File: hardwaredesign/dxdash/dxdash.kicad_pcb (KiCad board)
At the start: 2 copper layers, 133 parts, among them J1 Conn_01x08_Pin, J10 Screw_Terminal_01x04, J11 Screw_Terminal_01x04, J12 CAN, J16 uC_NRST, J17 3V3_uC, J18 SWO, J2 Conn_01x06_Pin, J3 Screw_Terminal_01x04, J4 DEBUG, J5 UART, J6 12V_in, J7 Screw_Terminal_01x04, J8 Power Low Side Outputs, J9 Screw_Terminal_01x04, Q1 NCV8402xST, Q2 NCV8402xST, Q3 NCV8402xST, Q4 BC556, Q6 BC546, Q7 BC556, Q8 BC546, SW1 SW_Push, SW2 SW_Push, SW3 SW_Push, SW4 SW_Push, SW5 SW_Push, U2 SN65HVD234, U3 STM32F103RETx, U4 TPS54302, U6 AMS1117-3.3, U7 74HCT04, Y2 8MHz

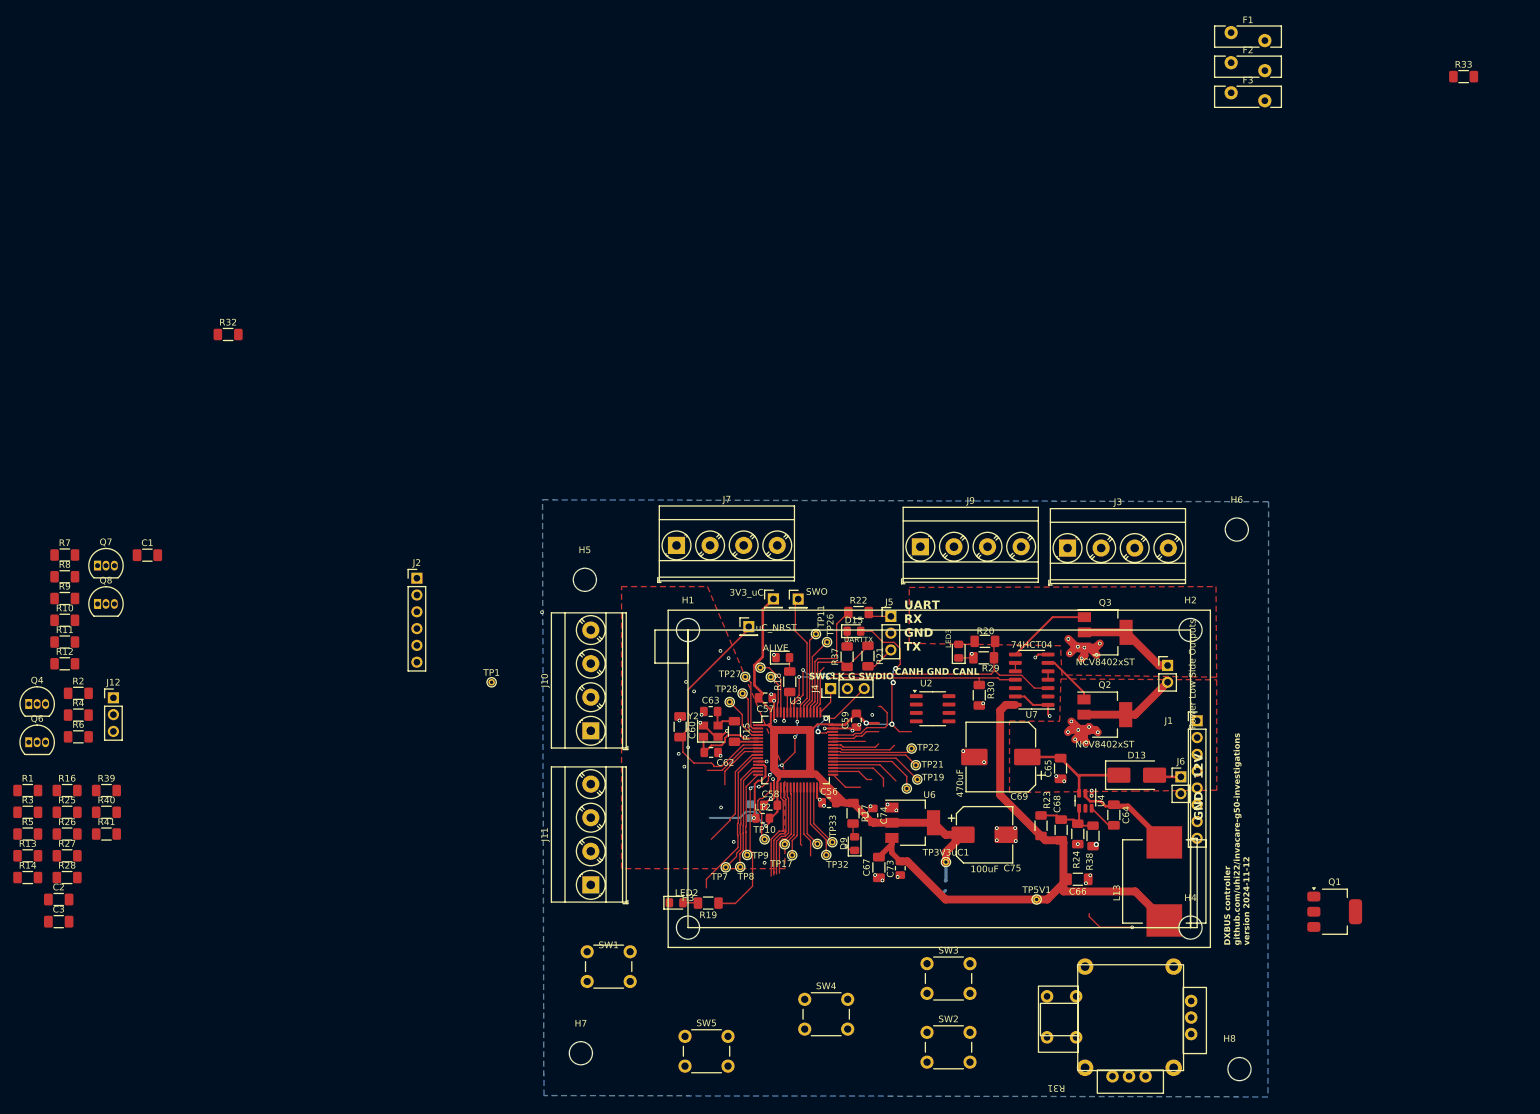
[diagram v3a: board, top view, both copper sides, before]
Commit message: added switch inputs. Layout preparation.
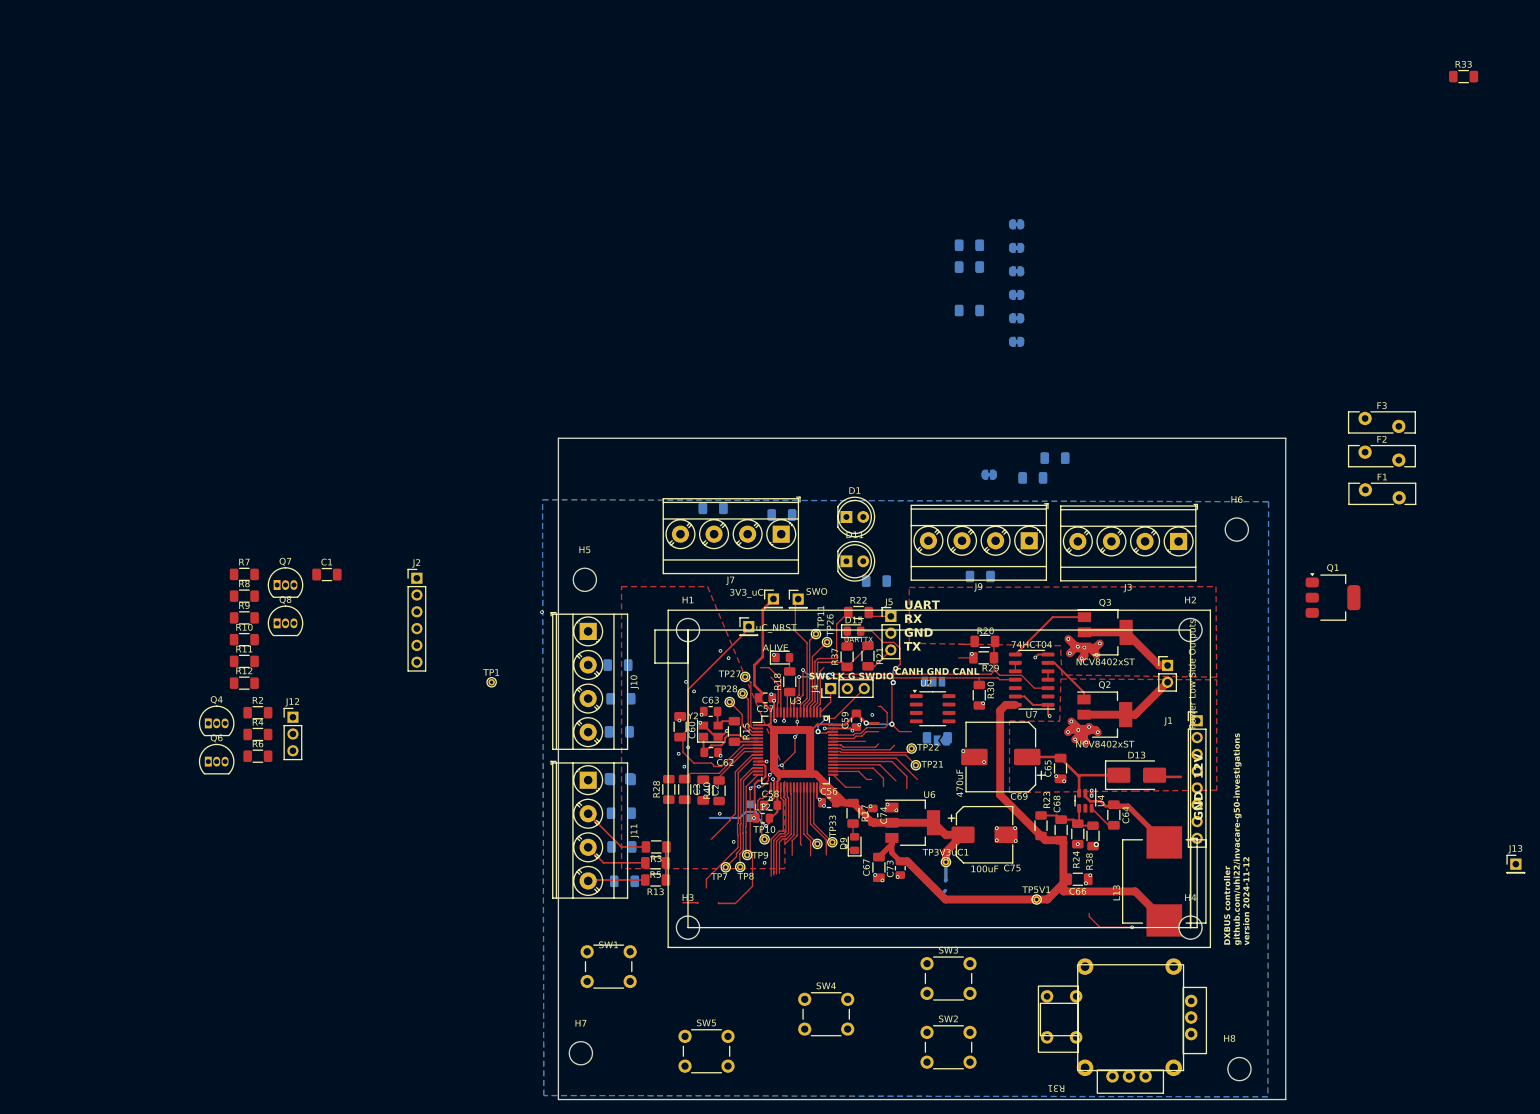
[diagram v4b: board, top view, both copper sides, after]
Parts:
- removed D12: LED3, LED_SMD:LED_0805_2012Metric_Pad1.15x1.40mm_HandSolder
- removed J6: 12V_in, Connector_PinHeader_2.54mm:PinHeader_1x02_P2.54mm_Vertical
- removed TP16, TP17, TP18, TP19, TP30, TP31, TP32: ~, TestPoint:TestPoint_THTPad_D1.0mm_Drill0.5mm
- added D1: LED2, LED_THT:LED_D5.0mm, F.Cu at (163.8, 71.7)
- added J13: Conn_01x01_Pin, Connector_PinHeader_2.54mm:PinHeader_1x01_P2.54mm_Vertical, F.Cu at (265.0, 124.2)
- added JP1: SolderJumper_2_Bridged, Jumper:SolderJumper-2_P1.3mm_Bridged_RoundedPad1.0x1.5mm, B.Cu at (189.5, 27.4)
- added JP2: SolderJumper_2_Bridged, Jumper:SolderJumper-2_P1.3mm_Bridged_RoundedPad1.0x1.5mm, B.Cu at (189.5, 31.0)
- added JP3: SolderJumper_2_Bridged, Jumper:SolderJumper-2_P1.3mm_Bridged_RoundedPad1.0x1.5mm, B.Cu at (189.5, 34.5)
- added JP4: SolderJumper_2_Open, Jumper:SolderJumper-2_P1.3mm_Open_TrianglePad1.0x1.5mm, B.Cu at (178.2, 105.5)
- added JP5: SolderJumper_3_Open, Jumper:SolderJumper-3_P1.3mm_Open_Pad1.0x1.5mm_NumberLabels, B.Cu at (176.9, 96.6)
- added JP6: SolderJumper_2_Bridged, Jumper:SolderJumper-2_P1.3mm_Bridged_RoundedPad1.0x1.5mm, B.Cu at (189.5, 38.1)
- added JP7: SolderJumper_2_Bridged, Jumper:SolderJumper-2_P1.3mm_Bridged_RoundedPad1.0x1.5mm, B.Cu at (189.5, 41.6)
- added JP8: SolderJumper_2_Bridged, Jumper:SolderJumper-2_P1.3mm_Bridged_RoundedPad1.0x1.5mm, B.Cu at (189.5, 45.2)
- added JP9: SolderJumper_2_Bridged, Jumper:SolderJumper-2_P1.3mm_Bridged_RoundedPad1.0x1.5mm, B.Cu at (185.4, 65.3)
- added R34: 47k, Resistor_SMD:R_1206_3216Metric_Pad1.30x1.75mm_HandSolder, B.Cu at (143.6, 70.4)
- added R35: 10k, Resistor_SMD:R_1206_3216Metric_Pad1.30x1.75mm_HandSolder, B.Cu at (182.4, 30.6)
- added R36: 10k, Resistor_SMD:R_1206_3216Metric_Pad1.30x1.75mm_HandSolder, B.Cu at (182.4, 33.9)
- added R42: 47k, Resistor_SMD:R_1206_3216Metric_Pad1.30x1.75mm_HandSolder, B.Cu at (154.0, 71.4)
- added R43: 10k, Resistor_SMD:R_1206_3216Metric_Pad1.30x1.75mm_HandSolder, B.Cu at (182.4, 40.4)
- added R44: 47k, Resistor_SMD:R_1206_3216Metric_Pad1.30x1.75mm_HandSolder, B.Cu at (184.0, 80.7)
- added R45: 10k, Resistor_SMD:R_1206_3216Metric_Pad1.30x1.75mm_HandSolder, B.Cu at (195.3, 62.8)
- added R46: 47k, Resistor_SMD:R_1206_3216Metric_Pad1.30x1.75mm_HandSolder, B.Cu at (192.0, 65.8)
- D11: footprint LED_SMD:LED_0805_2012Metric_Pad1.15x1.40mm_HandSolder -> LED_THT:LED_D5.0mm
- R1, R14, R16, R19, R25, R26, R27, R32, R39, R41: moved to B.Cu
- moved R32 123.4 mm to (177.5, 105.1)
- moved C2 98.9 mm to (142.1, 113.0), turned to -90 degrees
- moved C3 96.8 mm to (139.3, 112.9), turned to -90 degrees
- moved R3 95.2 mm to (135.0, 121.6), turned to 180 degrees
- moved R5 95.0 mm to (134.9, 124.0), turned to 180 degrees
- moved R13 95.0 mm to (134.9, 126.6), turned to 180 degrees
- moved R40 92.7 mm to (144.5, 113.1), turned to 90 degrees
- moved R28 92.0 mm to (136.9, 112.9), turned to 90 degrees
- moved R14 90.3 mm to (130.2, 126.8), turned to 180 degrees
- moved R1 89.8 mm to (129.7, 111.4)
- moved R27 88.2 mm to (129.2, 94.1), turned to 180 degrees
- moved R16 84.3 mm to (129.8, 121.6), turned to 180 degrees
- moved R26 83.9 mm to (129.4, 111.3), turned to 180 degrees
- moved R25 83.8 mm to (129.7, 116.5), turned to 180 degrees
- moved R41 79.1 mm to (129.4, 104.2), turned to 180 degrees
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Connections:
- J7 pad 3: unconnected-(J7-Pin_3-Pad3) -> switch1
- J7 pad 4: unconnected-(J7-Pin_4-Pad4) -> switch2
- J9 pad 3: unconnected-(J9-Pin_3-Pad3) -> switch3
- J9 pad 4: unconnected-(J9-Pin_4-Pad4) -> switch4
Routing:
- net button2: track 0.00 -> 10.8 mm
- net button3: track 0.00 -> 9.62 mm
- net button4: track 0.00 -> 8.71 mm
- net 3V3_uC: track 164.2 -> 169.2 mm
- net uC_pot1: track 9.05 -> 13.0 mm
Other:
- board outline added: 110 x 100 mm

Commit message: more layout
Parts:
- removed J12: CAN, Connector_PinHeader_2.54mm:PinHeader_1x03_P2.54mm_Vertical
- removed J2: Conn_01x06_Pin, Connector_PinHeader_2.54mm:PinHeader_1x06_P2.54mm_Vertical
- removed J8: Power Low Side Outputs, Connector_PinHeader_2.54mm:PinHeader_1x02_P2.54mm_Vertical
- C1, R11, R12, R2, R20, R29, R30, R33, R4, R6, U7: moved to B.Cu
- moved R7 169.1 mm to (234.9, 128.4)
- moved R8 166.1 mm to (229.4, 138.9), turned to 180 degrees
- moved Q8 157.2 mm to (227.8, 134.6)
- moved R9 157.1 mm to (225.7, 122.8)
- moved R10 156.2 mm to (223.7, 130.5), turned to 180 degrees
- moved Q7 153.0 mm to (223.9, 127.0)
- moved R33 117.8 mm to (193.1, 104.0), turned to 180 degrees
- moved Q4 109.8 mm to (176.8, 111.4)
- moved Q6 108.4 mm to (175.7, 106.4)
- moved R4 105.3 mm to (179.6, 114.1)
- moved R2 103.2 mm to (177.9, 105.2), turned to 180 degrees
- moved R6 94.7 mm to (169.3, 112.7), turned to 180 degrees
- moved JP3 91.6 mm to (156.6, 120.0), turned to -90 degrees
- moved JP6 84.9 mm to (154.5, 115.5), turned to 90 degrees
- moved JP7 80.6 mm to (157.1, 115.5), turned to -90 degrees
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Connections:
- J7 pad 1: OUT3_LS -> switch1
- J7 pad 2: unconnected-(J7-Pin_2-Pad2) -> switch2
- J7 pad 3: switch1 -> switch3
- J7 pad 4: switch2 -> switch4
- J9 pad 1: CANH -> OUT3_LS
- J9 pad 3: switch3 -> CANH
- J9 pad 4: switch4 -> unconnected-(J9-Pin_4-Pad4)
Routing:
- net (no net): track 98.2 -> 8.25 mm, vias 5 -> 1
- net GND: track 60.2 -> 25.3 mm, vias 70 -> 52
- net 5V: track 90.5 -> 75.1 mm
- net Net-(Q3-G): track 12.8 -> 0.00 mm
- net Net-(F1-Pad1): track 0.00 -> 12.1 mm
- net LED3: track 0.00 -> 11.7 mm, vias 0 -> 2
- net Net-(F3-Pad1): track 0.00 -> 11.4 mm
- net Net-(F2-Pad1): track 0.00 -> 11.0 mm
- net OUT3_LS: track 0.00 -> 10.4 mm
- net Net-(U3-PB6): track 0.00 -> 10.3 mm, vias 0 -> 2
- net Net-(JP9-B): track 14.1 -> 4.09 mm
- net Net-(Q2-G): track 8.34 -> 0.00 mm
- net OUT1_LS: track 14.7 -> 8.57 mm
- net OUT2_LS: track 14.7 -> 9.12 mm
- net Net-(U3-PC8): track 13.2 -> 9.14 mm
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- removed copper zone on F.Cu, net OUT1_LS
- removed copper zone on F.Cu, net OUT2_LS
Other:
- board size 110 x 100 mm -> 111.5 x 90.6 mm

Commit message: layout work in progress
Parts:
- removed TP3V3uC1: TP3V3uC, TestPoint:TestPoint_THTPad_D1.0mm_Drill0.5mm
- R1: moved to F.Cu
- R10, R7, R9: moved to B.Cu
- moved R32 52.5 mm to (203.8, 150.5), turned to 180 degrees
- moved R8 51.0 mm to (189.2, 107.4)
- moved Q8 43.5 mm to (197.0, 103.9), turned to 180 degrees
- moved R7 41.0 mm to (201.7, 104.3), turned to 90 degrees
- moved Q7 35.0 mm to (201.3, 100.2), turned to 90 degrees
- moved R10 31.4 mm to (204.4, 105.7), turned to -90 degrees
- moved D13 31.1 mm to (222.9, 83.6), turned to 90 degrees
- moved R9 30.7 mm to (204.4, 100.6), turned to 90 degrees
- moved C69 22.7 mm to (209.3, 103.1), turned to 90 degrees
- moved Q4 22.3 mm to (196.1, 100.3), turned to 90 degrees
- moved R6 22.0 mm to (186.7, 99.3)
- moved C66 16.9 mm to (182.3, 122.8), turned to 0 degrees
- moved Q6 16.6 mm to (191.0, 100.2), turned to 90 degrees
- moved R30 16.0 mm to (198.3, 91.9)
- moved R4 15.8 mm to (190.5, 102.7)
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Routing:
- net Net-(R10-Pad2): track 0.00 -> 121.2 mm, vias 0 -> 2
- net button2: track 10.8 -> 126.8 mm
- net uC_joystickX: track 16.2 -> 123.8 mm, vias 0 -> 2
- net uC_button1: track 6.31 -> 103.6 mm, vias 0 -> 9
- net button1: track 0.00 -> 93.3 mm
- net uC_joystickY: track 23.4 -> 105.4 mm, vias 0 -> 2
- net uC_pwr_button: track 4.90 -> 84.6 mm, vias 0 -> 1
- net SPI1_CLK: track 14.7 -> 88.2 mm, vias 0 -> 6
- net SPI1_MOSI: track 14.1 -> 84.7 mm, vias 0 -> 6
- net DISPLAY_DC: track 8.82 -> 77.3 mm, vias 0 -> 6
- net DISPLAY_RES: track 10.8 -> 74.6 mm, vias 0 -> 6
- net uC_button2: track 8.77 -> 69.2 mm, vias 0 -> 3
- net uC_button3: track 10.5 -> 69.8 mm, vias 0 -> 1
- net button3: track 9.62 -> 65.5 mm
- net CANH: track 0.00 -> 44.5 mm, vias 0 -> 4
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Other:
- board size 111.5 x 90.6 mm -> 104.6 x 90.6 mm

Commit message: more layout
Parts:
- moved TP1 50.8 mm to (160.8, 94.1)
- moved R46 39.8 mm to (137.4, 78.9)
- moved R44 37.4 mm to (145.2, 79.3)
- moved R43 36.9 mm to (143.0, 79.2)
- moved R45 34.0 mm to (140.6, 79.1)
- moved R34 11.8 mm to (154.7, 79.2)
- moved R42 10.4 mm to (148.0, 79.4)
- moved R36 10.0 mm to (150.2, 79.3)
- moved R35 7.00 mm to (152.5, 79.2)
- moved JP7 6.80 mm to (153.9, 121.5), turned to 0 degrees
- moved JP1 5.96 mm to (152.3, 94.9), turned to 90 degrees
- moved JP6 3.73 mm to (154.0, 119.2)
- moved JP5 3.51 mm to (173.4, 96.8)
- moved U2 3.31 mm to (173.5, 100.9)
- moved JP2 2.82 mm to (150.5, 94.8)
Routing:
- net 5V: track 32.8 -> 124.0 mm, vias 0 -> 3
- net uC_joystickbutton: track 30.0 -> 95.7 mm, vias 0 -> 4
- net uC_switch1: track 0.00 -> 65.6 mm, vias 0 -> 2
- net OUT_CONTROL2: track 3.31 -> 63.3 mm, vias 0 -> 6
- net uC_switch2: track 0.00 -> 51.2 mm, vias 0 -> 2
- net uC_switch4: track 0.00 -> 42.5 mm
- net uC_switch3: track 0.00 -> 42.5 mm
- net 3V3_uC: track 169.2 -> 209.8 mm
- net OUT_CONTROL3: track 3.97 -> 44.1 mm, vias 0 -> 2
- net OUT_CONTROL1: track 17.8 -> 52.9 mm, vias 1 -> 4
- net Net-(R10-Pad2): track 121.2 -> 87.4 mm
- net LED3: track 12.5 -> 36.3 mm, vias 2 -> 1
- net GND: track 33.5 -> 51.4 mm, vias 48 -> 53
- net Net-(JP5-C): track 0.00 -> 7.99 mm, vias 0 -> 1
- net switch4: track 0.00 -> 6.85 mm
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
